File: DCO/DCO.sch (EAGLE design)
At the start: 17 parts, among them IC1 PIC16F18325SL, IC2 MAX5216, IC3 TL082D, Q1 MMBT3906

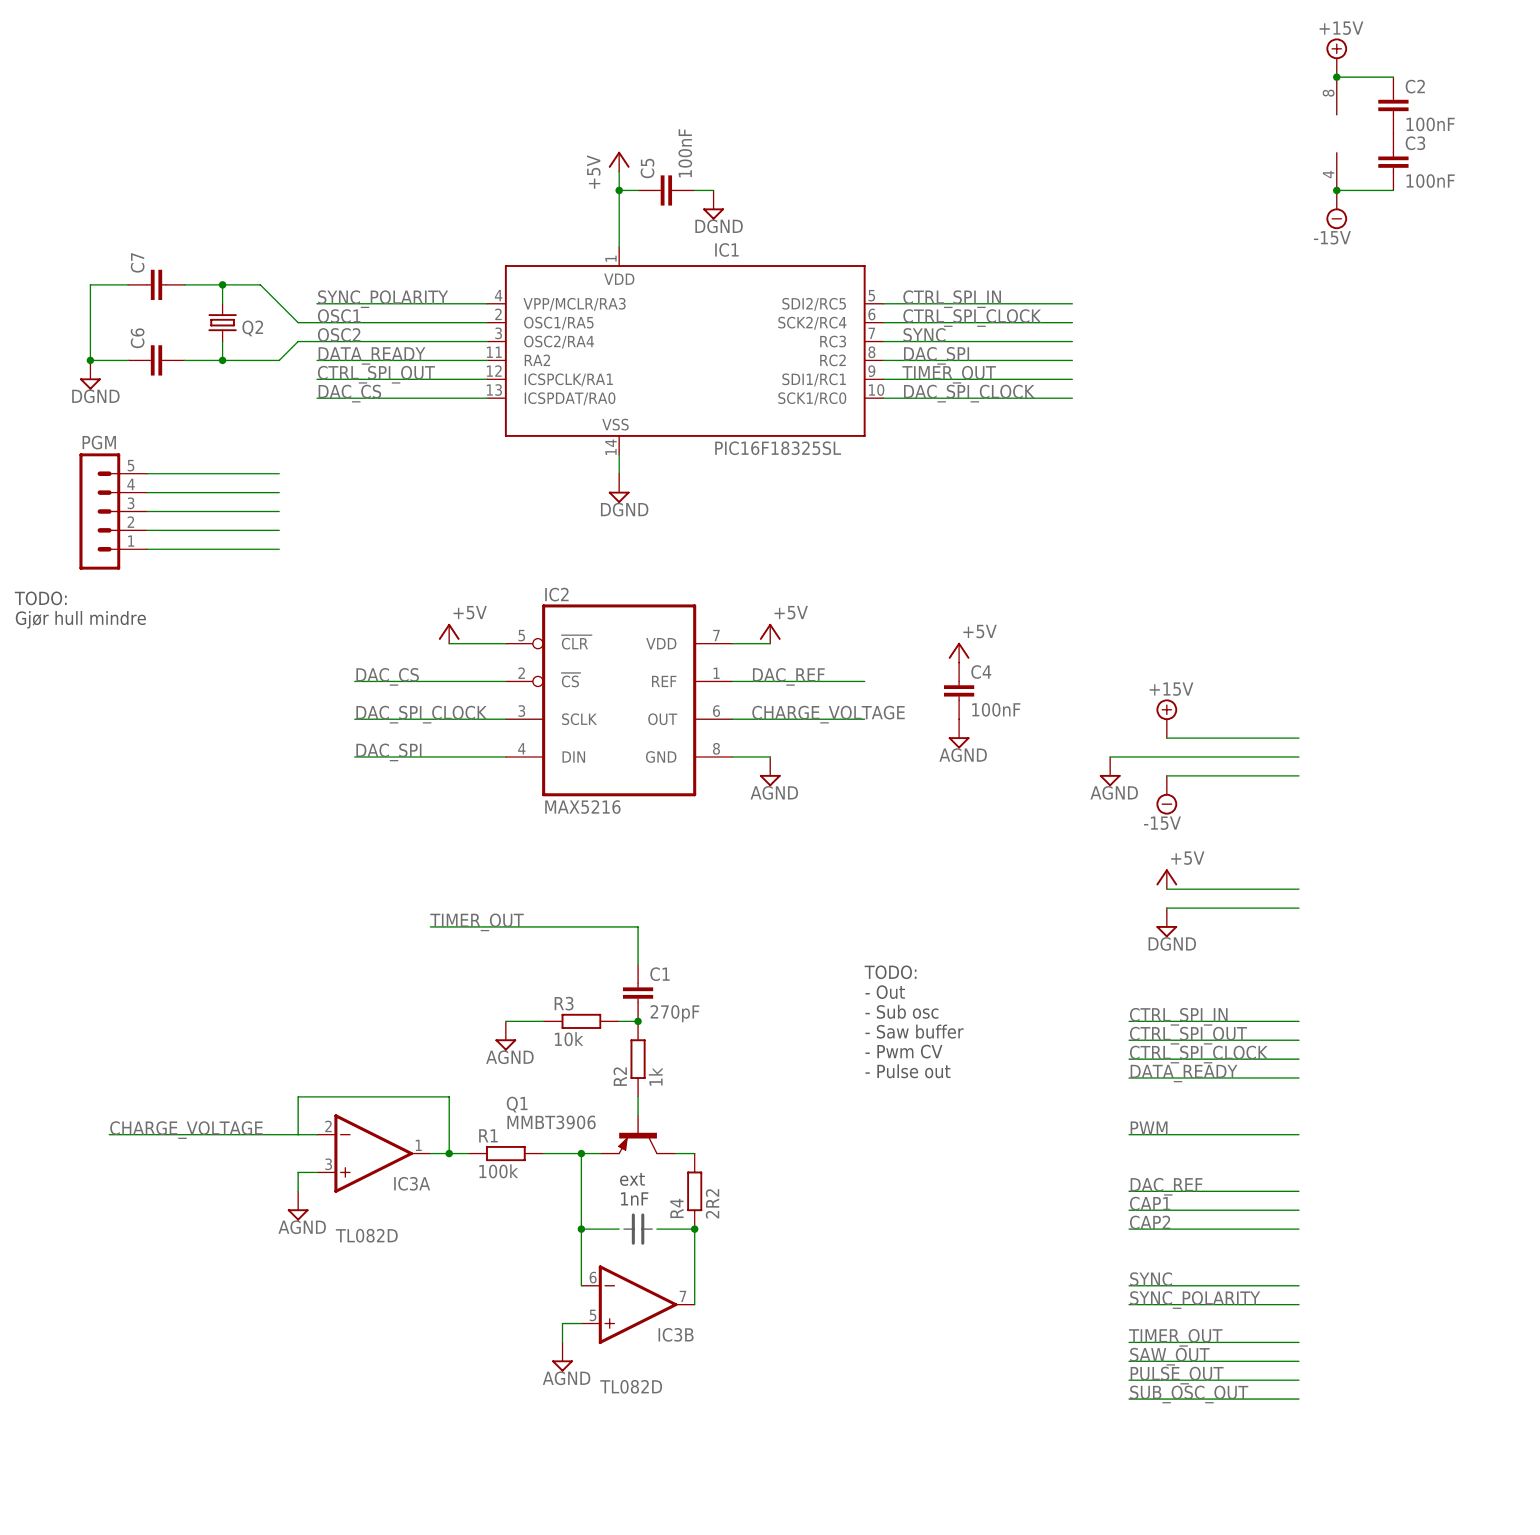
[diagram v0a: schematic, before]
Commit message: Layout for DCO core completed
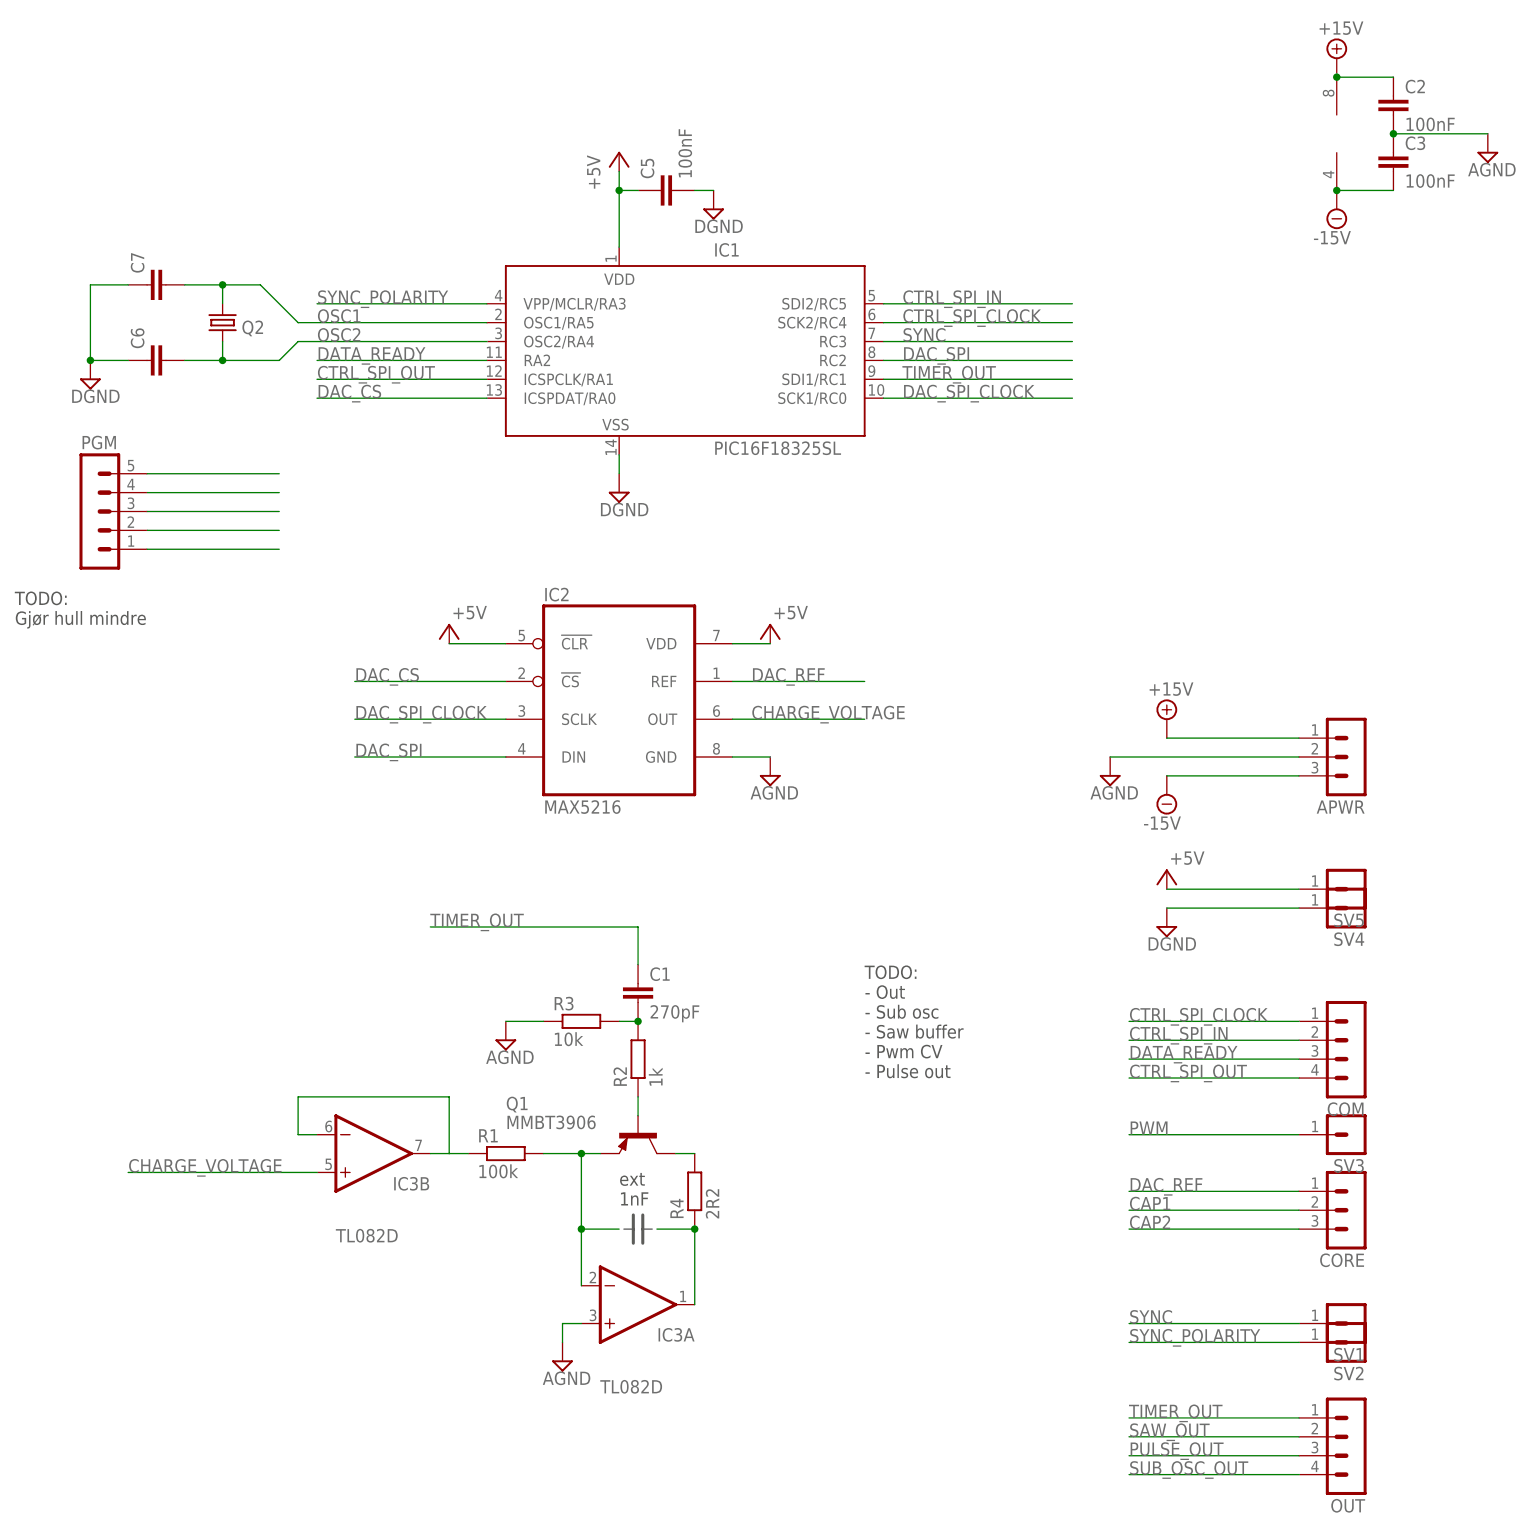
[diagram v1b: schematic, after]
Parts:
- removed C4: 100nF, resistor:C-EUC0805
- added APWR, CORE: (no value), joakim:MA03-1J
- added COM, OUT: (no value), joakim:MA04-1J
- added SV1, SV2, SV3, SV4, SV5: (no value), joakim:MA01-1J
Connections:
- removed net N$1: C2.2, C3.1
- new net N$10: IC3B.-IN, IC3B.OUT, R1.1
- new net PULSE_OUT: OUT.3
- new net PWM: SV3.1
- new net SAW_OUT: OUT.2
- new net SUB_OSC_OUT: OUT.4
- net +15V: now also APWR.1
- net +5V: now also SV5.1; no longer C4.1
- net -15V: now also APWR.3
- net AGND: now also APWR.2, C2.2, C3.1; no longer C4.2, IC3B.+IN
- net CAP1: now also CORE.2, IC3A.-IN; no longer IC3B.-IN
- net CAP2: now also CORE.3, IC3A.OUT; no longer IC3B.OUT
- net CHARGE_VOLTAGE: now also IC3B.+IN; no longer IC3A.-IN, IC3A.OUT, R1.1
- net CTRL_SPI_CLOCK: now also COM.1
- net CTRL_SPI_IN: now also COM.2
- net CTRL_SPI_OUT: now also COM.4
- net DAC_REF: now also CORE.1
- net DATA_READY: now also COM.3
- net DGND: now also SV4.1
- net SYNC: now also SV1.1
- net SYNC_POLARITY: now also SV2.1
- net TIMER_OUT: now also OUT.1
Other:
- moved on the sheet: IC3A, IC3B
